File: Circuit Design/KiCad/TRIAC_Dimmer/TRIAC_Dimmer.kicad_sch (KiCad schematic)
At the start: 17 parts, among them J1 1726480102, J2 1726480102, Q1 BT136-600

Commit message: PCB libraries were global, made them local
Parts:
- removed C1: B32672L6104K000, Personal_Capacitor_THT:CAPRR1500W80L1800T700H1250, symbol Personal_Capacitor_THT:B32672L6104K000
- removed F1: 05200101Z, Personal_Fuses:FUSE_05200101Z_LTF, symbol Personal_Fuses:05200101Z
- removed J1, J2: 1726480102, Personal_Connector_THT:CONN_SD-172648-0000_02_MOL, symbol Personal_Connector_THT:1726480102
- removed Q1: BT136-600, Package_TO_SOT_THT:TO-220-3_Vertical, symbol Triac_Thyristor:BT136-600
- removed TP1, TP2, TP3, TP4: 5271, Personal_Test_Point_THT:KEYSTONE_5271, symbol Personal_Test_Point_THT:5271
- added C1: 0.1uF, CAPRR1500W80L1800T700H1250:CAPRR1500W80L1800T700H1250, symbol B32672L6104K000:B32672L6104K000
- added CR1: BTB04-600SL, TO-220AB_STM:TO-220AB_STM, symbol BTB04-600SL:BTB04-600SL
- added F1: 05200101Z, FUSE_05200101Z_LTF:FUSE_05200101Z_LTF, symbol 05200101Z:05200101Z
- added J1, J2: Screw_Terminal_01x02, TerminalBlock_Phoenix:TerminalBlock_Phoenix_MKDS-1,5-2-5.08_1x02_P5.08mm_Horizontal, symbol Connector:Screw_Terminal_01x02
- added TP1, TP2, TP3, TP4: 5271, KEYSTONE_5271:KEYSTONE_5271, symbol 5271:5271
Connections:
- net at R1.2, R2.1, RV1.3: now also TP3.1
- net at D1.1 (K), R2.2: now also C1.1, TP4.1
- net at R1.1, RV1.1, RV1.2: now also CR1.2, F1.2, TP1.1
- net at D1.2 (A): now also CR1.3
- new net: J1.1 (Pin_1), J2.2 (Pin_2)
- new net: C1.2, CR1.1, J1.2 (Pin_2), TP2.1
- new net: F1.1, J2.1 (Pin_1)
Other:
- moved on the sheet: H1, H2, H3, H4

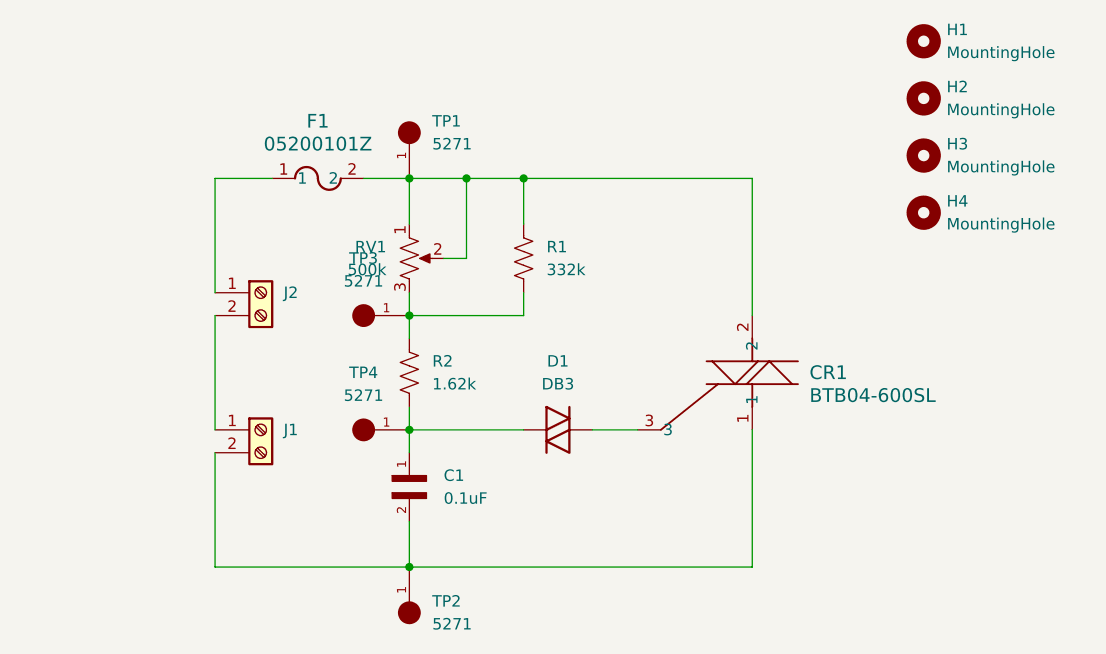
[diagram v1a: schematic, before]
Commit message: Rough layout complete
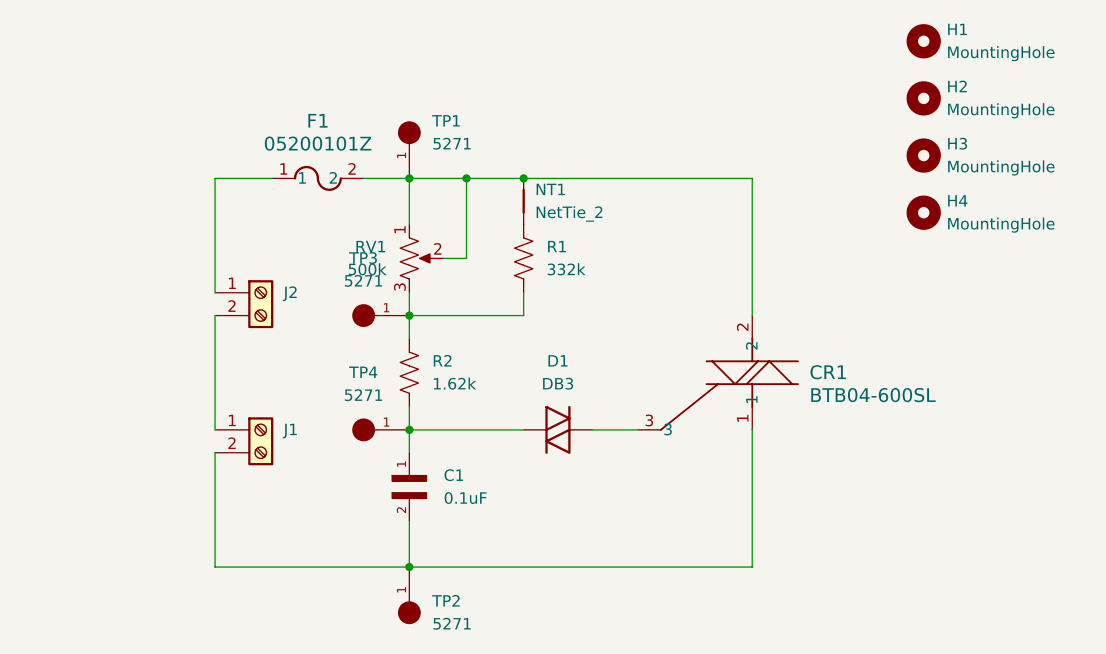
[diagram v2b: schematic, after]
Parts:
- added NT1: NetTie_2, NetTie:NetTie-2_SMD_Pad0.5mm, symbol Device:NetTie_2
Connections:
- net at CR1.2, F1.2, RV1.1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: now also NT1.2; no longer R1.1
- new net: NT1.1, R1.1
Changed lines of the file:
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@@
+	)
+	(junction
+		(at 152.4 74.93)
+		(diameter 0)
+		(color 0 0 0 0)
 	)
 	(junction
@@
 	)
 	(junction
-		(at 152.4 74.93)
+		(at 139.7 118.11)
 		(diameter 0)
 		(color 0 0 0 0)
 	)
 	(junction
-		(at 139.7 118.11)
+		(at 139.7 90.17)
 		(diameter 0)
 		(color 0 0 0 0)
@@
 		(color 0 0 0 0)
 	)
-	(junction
-		(at 139.7 90.17)
-		(diameter 0)
-		(color 0 0 0 0)
-	)
 	(wire
 		(pts
@@
 	(wire
 		(pts
+			(xy 146.05 74.93) (xy 152.4 74.93)
+		)
+		(stroke
+			(width 0)
+			(type default)
+		)
+	)
+	(wire
+		(pts
+			(xy 139.7 90.17) (xy 139.7 92.71)
+		)
+		(stroke
+			(width 0)
+			(type default)
+		)
+	)
+	(wire
+		(pts
+			(xy 139.7 102.87) (xy 139.7 105.41)
+		)
+		(stroke
+			(width 0)
+			(type default)
+		)
+	)
+	(wire
+		(pts
+			(xy 139.7 102.87) (xy 152.4 102.87)
+		)
+		(stroke
+			(width 0)
+			(type default)
+		)
+	)
+	(wire
+		(pts
+			(xy 177.8 74.93) (xy 177.8 90.17)
+		)
+		(stroke
+			(width 0)
+			(type default)
+		)
+	)
+	(wire
+		(pts
+			(xy 139.7 74.93) (xy 146.05 74.93)
+		)
+		(stroke
+			(width 0)
+			(type default)
+		)
+	)
+	(wire
+		(pts
+			(xy 118.11 118.11) (xy 118.11 105.41)
+		)
+		(stroke
+			(width 0)
+			(type default)
+		)
+	)
+	(wire
+		(pts
+			(xy 160.02 102.87) (xy 165.1 102.87)
+		)
+		(stroke
+			(width 0)
+			(type default)
+		)
+	)
+	(wire
+		(pts
+			(xy 146.05 83.82) (xy 146.05 74.93)
+		)
+		(stroke
+			(width 0)
+			(type default)
+		)
+	)
+	(wire
+		(pts
+			(xy 139.7 74.93) (xy 139.7 80.01)
+		)
+		(stroke
+			(width 0)
+			(type default)
+		)
+	)
+	(wire
+		(pts
+			(xy 152.4 90.17) (xy 139.7 90.17)
+		)
+		(stroke
+			(width 0)
+			(type default)
+		)
+	)
+	(wire
+		(pts
+			(xy 139.7 87.63) (xy 139.7 90.17)
+		)
+		(stroke
+			(width 0)
+			(type default)
+		)
+	)
+	(wire
+		(pts
+			(xy 177.8 102.87) (xy 177.8 118.11)
+		)
+		(stroke
+			(width 0)
+			(type default)
+		)
+	)
+	(wire
+		(pts
+			(xy 134.62 74.93) (xy 139.7 74.93)
+		)
+		(stroke
+			(width 0)
+			(type default)
+		)
+	)
+	(wire
+		(pts
+			(xy 118.11 90.17) (xy 118.11 102.87)
+		)
+		(stroke
+			(width 0)
+			(type default)
+		)
+	)
+	(wire
+		(pts
+			(xy 152.4 87.63) (xy 152.4 90.17)
+		)
+		(stroke
+			(width 0)
+			(type default)
+		)
+	)
+	(wire
+		(pts
+			(xy 118.11 74.93) (xy 118.11 87.63)
+		)
+		(stroke
+			(width 0)
+			(type default)
+		)
+	)
+	(wire
+		(pts
+			(xy 139.7 118.11) (xy 177.8 118.11)
+		)
+		(stroke
+			(width 0)
+			(type default)
+		)
+	)
+	(wire
+		(pts
 			(xy 152.4 74.93) (xy 177.8 74.93)
-		)
-		(stroke
-			(width 0)
-			(type default)
-		)
-	)
-	(wire
-		(pts
-			(xy 139.7 90.17) (xy 139.7 92.71)
-		)
-		(stroke
-			(width 0)
-			(type default)
-		)
-	)
-	(wire
-		(pts
-			(xy 139.7 102.87) (xy 139.7 105.41)
-		)
-		(stroke
-			(width 0)
-			(type default)
-		)
-	)
-	(wire
-		(pts
-			(xy 139.7 102.87) (xy 152.4 102.87)
-		)
-		(stroke
-			(width 0)
-			(type default)
-		)
-	)
-	(wire
-		(pts
-			(xy 177.8 74.93) (xy 177.8 90.17)
-		)
-		(stroke
-			(width 0)
-			(type default)
-		)
-	)
-	(wire
-		(pts
-			(xy 139.7 74.93) (xy 146.05 74.93)
-		)
-		(stroke
-			(width 0)
-			(type default)
-		)
-	)
-	(wire
-		(pts
-			(xy 118.11 118.11) (xy 118.11 105.41)
-		)
-		(stroke
-			(width 0)
-			(type default)
-		)
-	)
-	(wire
-		(pts
-			(xy 160.02 102.87) (xy 165.1 102.87)
-		)
-		(stroke
-			(width 0)
-			(type default)
-		)
-	)
-	(wire
-		(pts
-			(xy 146.05 83.82) (xy 146.05 74.93)
-		)
-		(stroke
-			(width 0)
-			(type default)
-		)
-	)
-	(wire
-		(pts
-			(xy 139.7 74.93) (xy 139.7 80.01)
-		)
-		(stroke
-			(width 0)
-			(type default)
-		)
-	)
-	(wire
-		(pts
-			(xy 152.4 90.17) (xy 139.7 90.17)
-		)
-		(stroke
-			(width 0)
-			(type default)
-		)
-	)
-	(wire
-		(pts
-			(xy 139.7 87.63) (xy 139.7 90.17)
-		)
-		(stroke
-			(width 0)
-			(type default)
-		)
-	)
-	(wire
-		(pts
-			(xy 177.8 102.87) (xy 177.8 118.11)
-		)
-		(stroke
-			(width 0)
-			(type default)
-		)
-	)
-	(wire
-		(pts
-			(xy 146.05 74.93) (xy 152.4 74.93)
-		)
-		(stroke
-			(width 0)
-			(type default)
-		)
-	)
-	(wire
-		(pts
-			(xy 134.62 74.93) (xy 139.7 74.93)
-		)
-		(stroke
-			(width 0)
-			(type default)
-		)
-	)
-	(wire
-		(pts
-			(xy 118.11 90.17) (xy 118.11 102.87)
-		)
-		(stroke
-			(width 0)
-			(type default)
-		)
-	)
-	(wire
-		(pts
-			(xy 152.4 87.63) (xy 152.4 90.17)
-		)
-		(stroke
-			(width 0)
-			(type default)
-		)
-	)
-	(wire
-		(pts
-			(xy 118.11 74.93) (xy 118.11 87.63)
-		)
-		(stroke
-			(width 0)
-			(type default)
-		)
-	)
-	(wire
-		(pts
-			(xy 139.7 118.11) (xy 177.8 118.11)
-		)
-		(stroke
-			(width 0)
-			(type default)
-		)
-	)
-	(wire
-		(pts
-			(xy 152.4 74.93) (xy 152.4 80.01)
 		)
 		(stroke
@@
 					(unit 1)
 				)
+			)
+		)
+	)
+	(symbol
+		(lib_id "Device:NetTie_2")
+		(at 152.4 77.47 90)
+		(unit 1)
+		(exclude_from_sim no)
+		(in_bom no)
+		(on_board yes)
+		(dnp no)
+		(fields_autoplaced yes)
+		(property "Reference" "NT1"
+			(at 153.67 76.1999 90)
+			(effects
+				(font
+					(size 1.27 1.27)
+				)
+				(justify right)
+			)
+		)
+		(property "Value" "NetTie_2"
+			(at 153.67 78.7399 90)
+			(effects
+				(font
+					(size 1.27 1.27)
+				)
+				(justify right)
+			)
+		)
+		(property "Footprint" "NetTie:NetTie-2_SMD_Pad0.5mm"
+			(at 152.4 77.47 0)
+			(effects
+				(font
+					(size 1.27 1.27)
+				)
+				(hide yes)
+			)
+		)
+		(property "Datasheet" "~"
+			(at 152.4 77.47 0)
+			(effects
+				(font
+					(size 1.27 1.27)
+				)
+				(hide yes)
+			)
+		)
+		(property "Description" "Net tie, 2 pins"
+			(at 152.4 77.47 0)
+			(effects
+				(font
+					(size 1.27 1.27)
+				)
+				(hide yes)
+			)
+		)
+		(pin "2"
+		)
+		(pin "1"
+		)
+		(instances
+			(project ""
+				(path "/d1613c86-1f6d-4698-aea0-80c55f6d8429"
+					(reference "NT1")
+					(unit 1)
+				)
